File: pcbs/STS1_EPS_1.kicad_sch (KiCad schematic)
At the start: 6 parts, among them J1 Inter-EPS, U12 BD50GA5WEFJ

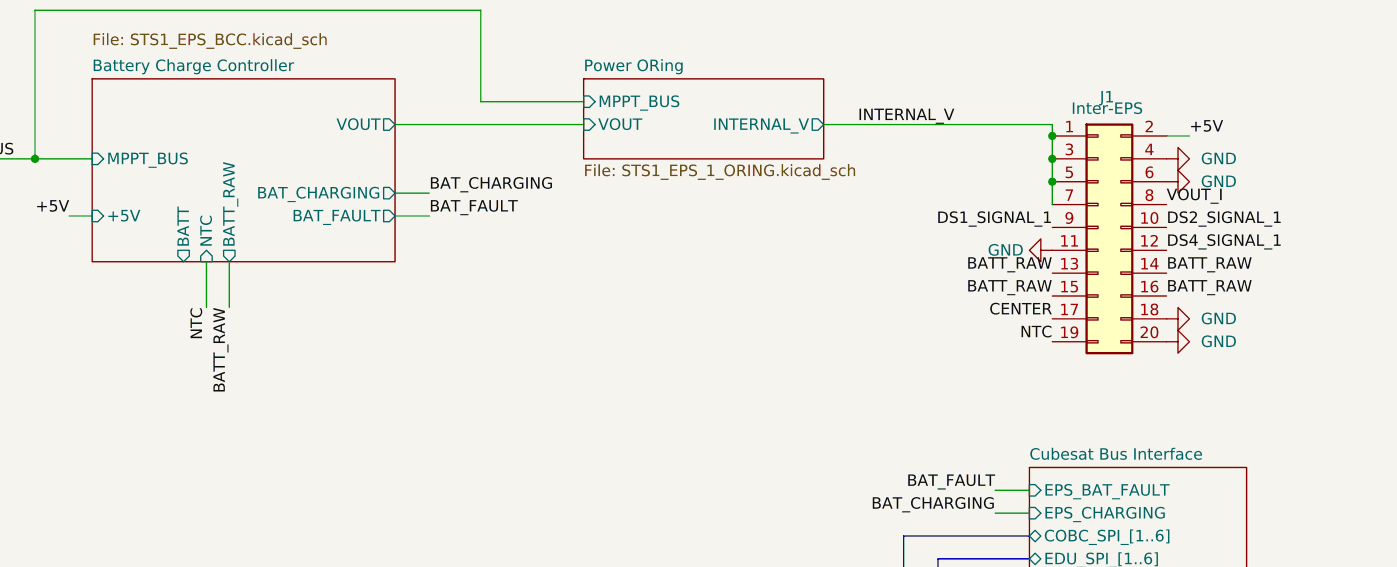
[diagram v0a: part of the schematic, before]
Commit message: Worked on STS1_EPS_1.
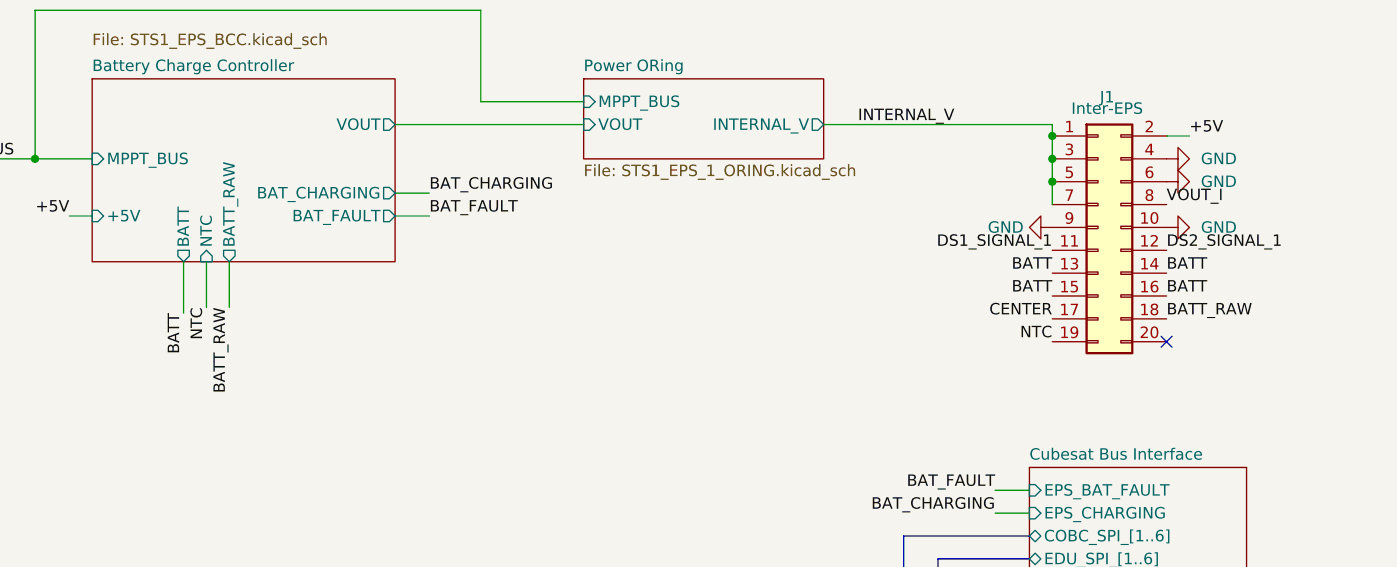
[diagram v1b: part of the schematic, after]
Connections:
- net DS4_SIGNAL_1 is gone; now on net DS2_SIGNAL_1: J1.12 (Pin_12)
- net BATT_RAW: now also J1.18 (Pin_18); no longer J1.13 (Pin_13), J1.14 (Pin_14), J1.15 (Pin_15), J1.16 (Pin_16)
- net DS1_SIGNAL_1: now also J1.11 (Pin_11); no longer J1.9 (Pin_9)
- net DS2_SIGNAL_1: no longer J1.10 (Pin_10)
- net GND: now also J1.10 (Pin_10), J1.9 (Pin_9); no longer J1.11 (Pin_11), J1.18 (Pin_18), J1.20 (Pin_20)
- new net BATT: J1.13 (Pin_13), J1.14 (Pin_14), J1.15 (Pin_15), J1.16 (Pin_16)
- no-connect marks 2 -> 3

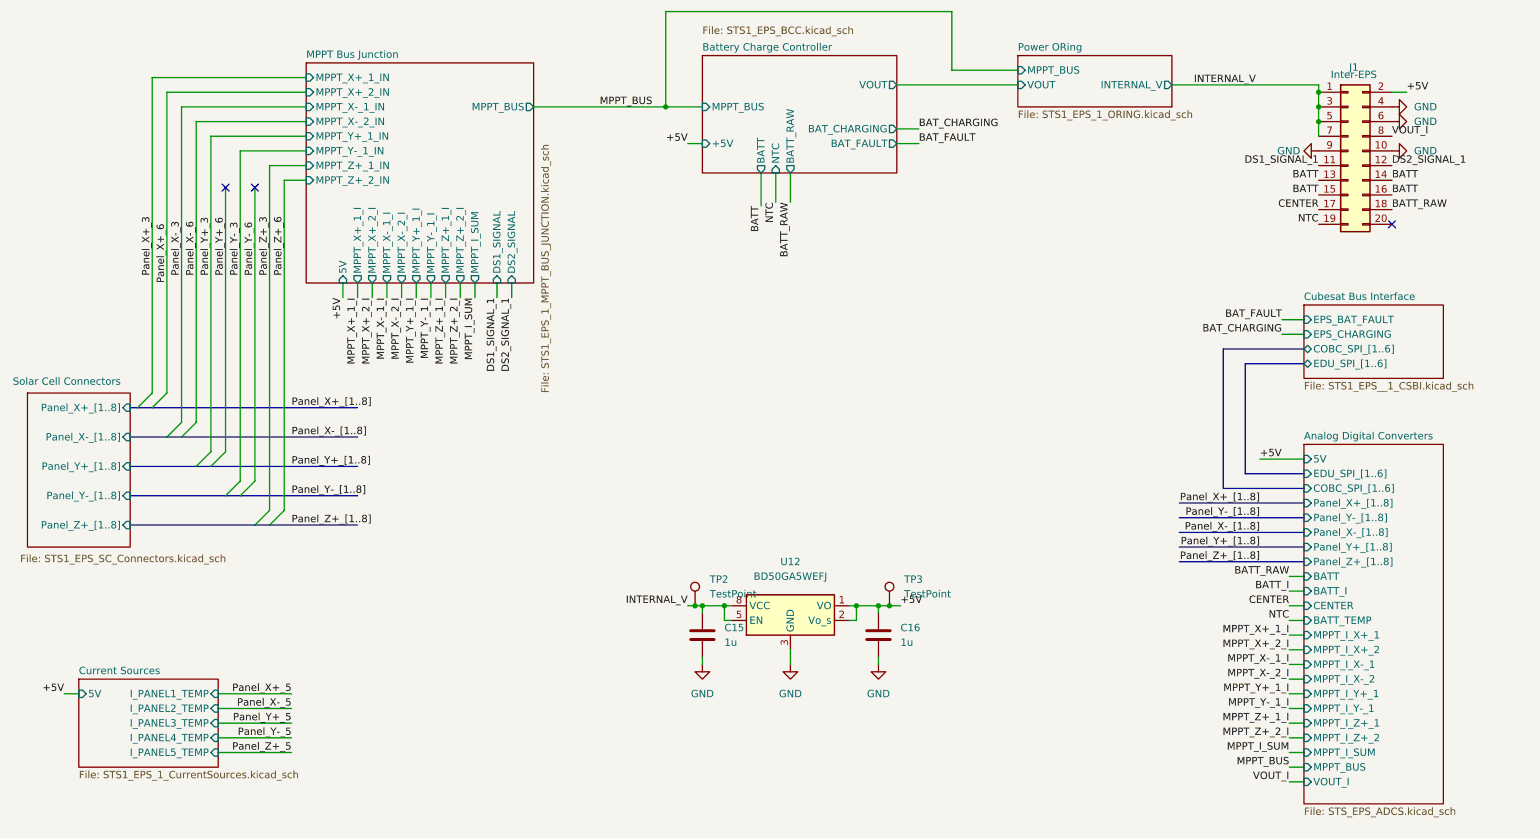
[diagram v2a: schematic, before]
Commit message: Worked on STS1_EPS_1.
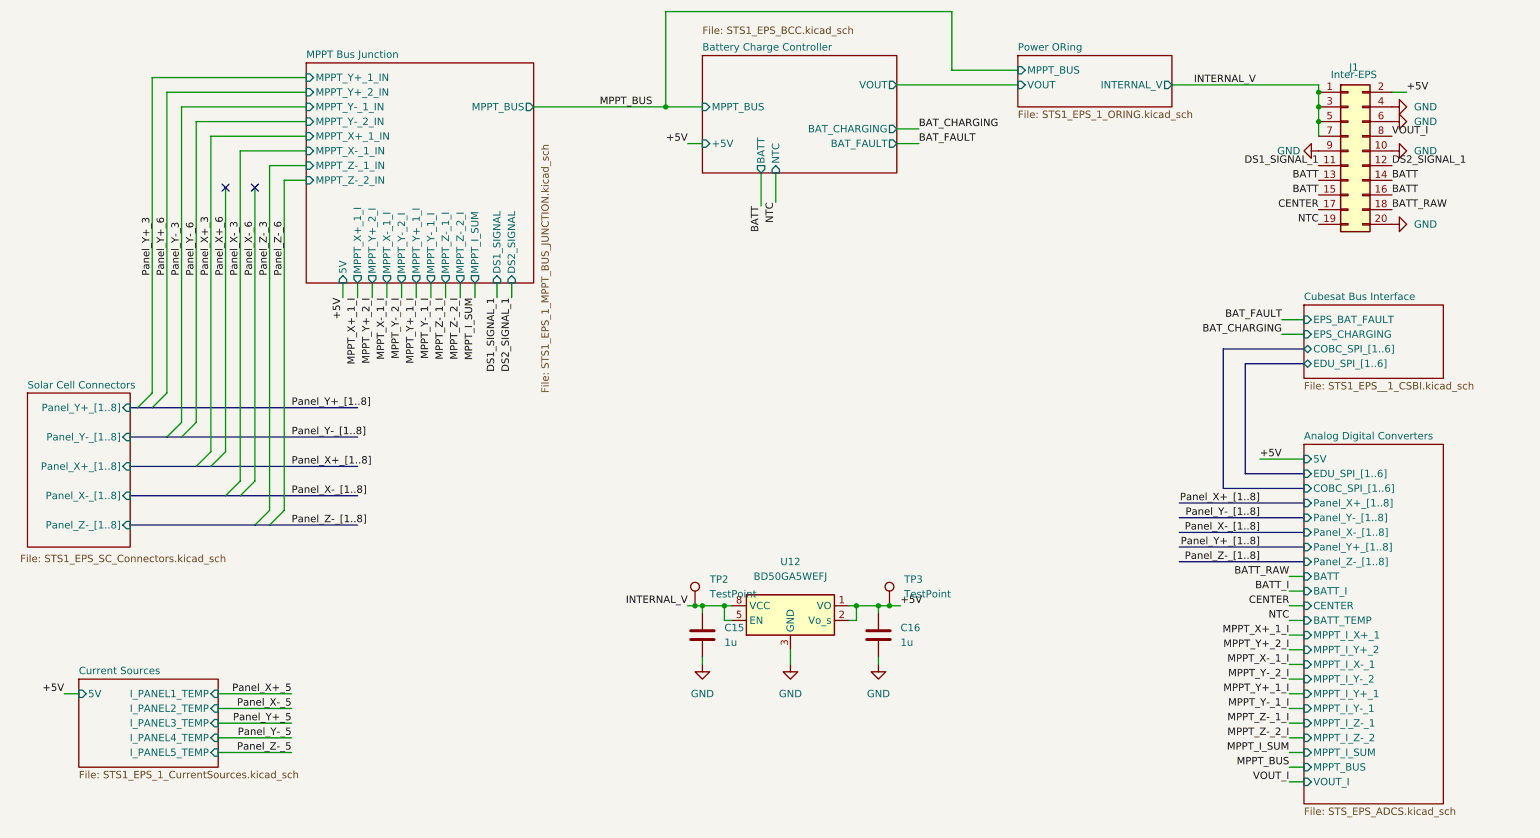
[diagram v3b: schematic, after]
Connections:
- net GND: now also J1.20 (Pin_20)
- no-connect marks 3 -> 2
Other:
- sheet Analog Digital Converters ports: added MPPT_I_Y+_2, MPPT_I_Y-_2, MPPT_I_Z-_1, MPPT_I_Z-_2, Panel_Z-_[1..8]; removed MPPT_I_X+_2, MPPT_I_X-_2, MPPT_I_Z+_1, MPPT_I_Z+_2, Panel_Z+_[1..8]
- sheet Battery Charge Controller ports: added none; removed BATT_RAW
- sheet MPPT Bus Junction ports: added MPPT_Y+_2_I, MPPT_Y+_2_IN, MPPT_Y-_2_I, MPPT_Y-_2_IN, MPPT_Z-_1_I, MPPT_Z-_1_IN, MPPT_Z-_2_I, MPPT_Z-_2_IN; removed MPPT_X+_2_I, MPPT_X+_2_IN, MPPT_X-_2_I, MPPT_X-_2_IN, MPPT_Z+_1_I, MPPT_Z+_1_IN, MPPT_Z+_2_I, MPPT_Z+_2_IN
- sheet Solar Cell Connectors ports: added Panel_Z-_[1..8]; removed Panel_Z+_[1..8]

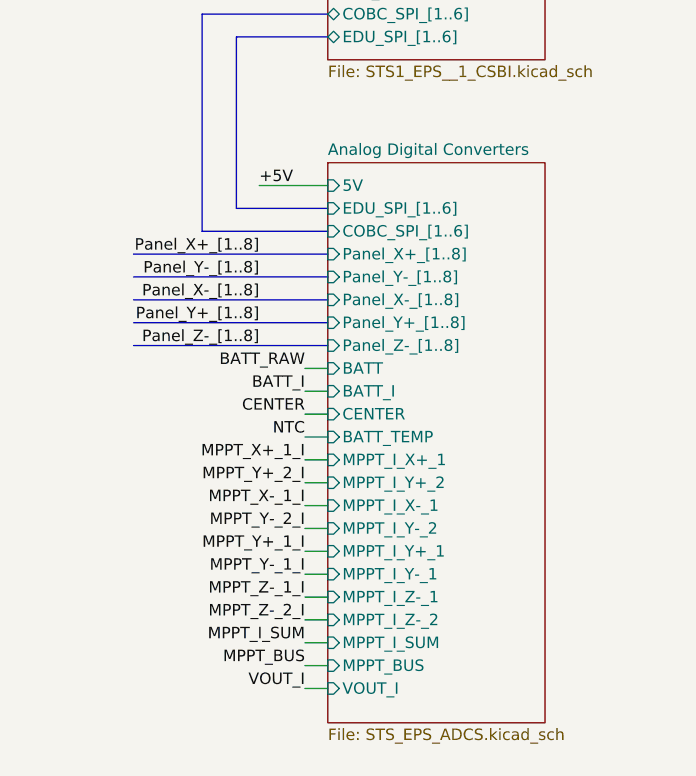
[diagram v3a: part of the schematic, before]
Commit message: Worked on STS1_EPS_1.
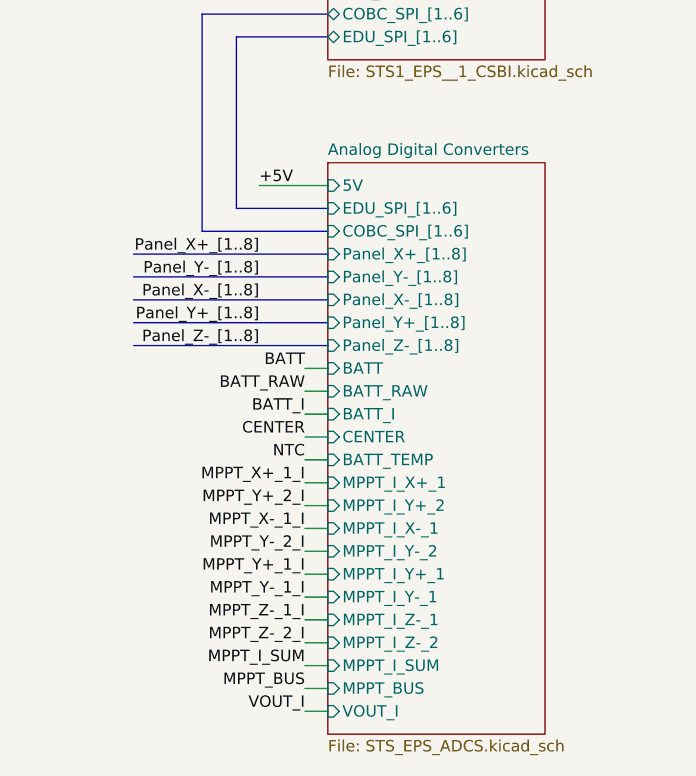
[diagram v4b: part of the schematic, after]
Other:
- sheet Analog Digital Converters ports: added BATT_RAW; removed none

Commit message: Worked on STS1_EPS_1 and STS1_EPS_2.
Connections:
- net BATT_I: now also J1.20 (Pin_20)
- net GND: no longer J1.20 (Pin_20)
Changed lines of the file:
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@@
+    (effects (font (size 1.27 1.27)) (justify left bottom))
+  )
+  (label "BATT_I" (at 250.19 54.61 0)
     (effects (font (size 1.27 1.27)) (justify left bottom))
   )
@@
     )
     (property "Datasheet" "" (id 3) (at 250.19 41.91 0)
-      (effects (font (size 1.27 1.27)) hide)
-    )
-    (pin "1")
-  )
-  (symbol (lib_id "power:GND") (at 250.19 54.61 90) (unit 1)
-    (in_bom yes) (on_board yes) (fields_autoplaced)
-    (property "Reference" "#PWR068" (id 0) (at 256.54 54.61 0)
-      (effects (font (size 1.27 1.27)) hide)
-    )
-    (property "Value" "GND" (id 1) (at 254 54.6099 90)
-      (effects (font (size 1.27 1.27)) (justify right))
-    )
-    (property "Footprint" "" (id 2) (at 250.19 54.61 0)
-      (effects (font (size 1.27 1.27)) hide)
-    )
-    (property "Datasheet" "" (id 3) (at 250.19 54.61 0)
       (effects (font (size 1.27 1.27)) hide)
     )
@@
       (reference "#PWR067") (unit 1) (value "GND") (footprint "")
     )
-    (path "/5715810c-7aee-4fb7-8ca7-e5bcf3201e81"
-      (reference "#PWR068") (unit 1) (value "GND") (footprint "")
-    )
     (path "/1fa7f756-57e9-4cd3-900e-1a1c84a07cba/6a3f3e97-3980-4780-a8e9-1ce1471695d7"

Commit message: Added a logic voltage, so that the deployment circuit breaker FETs also work, when battery is fails.
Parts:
- J1: footprint Connector_PinHeader_2.00mm:PinHeader_2x10_P2.00mm_Vertical -> Connector_PinHeader_2.00mm:PinHeader_2x11_P2.00mm_Vertical; symbol Connector_Generic:Conn_02x10_Odd_Even -> Connector_Generic:Conn_02x11_Odd_Even
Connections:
- new net MPPT_SUM: J1.22 (Pin_22)
- new net V_LOGIC: J1.21 (Pin_21)
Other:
- sheet MPPT Bus Junction ports: added MPPT_SUM; removed none
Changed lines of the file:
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@@
+    (stroke (width 0) (type default) (color 0 0 0 0))
+  )
+  (wire (pts (xy 101.6 36.83) (xy 103.505 36.83))
     (stroke (width 0) (type default) (color 0 0 0 0))
   )
@@
     (effects (font (size 1.27 1.27)) (justify right bottom))
   )
+  (label "MPPT_SUM" (at 250.19 57.15 0)
+    (effects (font (size 1.27 1.27)) (justify left bottom))
+  )
   (label "MPPT_X-_1_I" (at 76.2 67.31 270)
     (effects (font (size 1.27 1.27)) (justify right bottom))
@@
     (effects (font (size 1.27 1.27)) (justify left bottom))
   )
+  (label "MPPT_SUM" (at 103.505 36.83 0)
+    (effects (font (size 1.27 1.27)) (justify left bottom))
+  )
   (label "BATT_RAW" (at 232.41 118.11 180)
     (effects (font (size 1.27 1.27)) (justify right bottom))
@@
   (label "DS2_SIGNAL_1" (at 250.19 44.45 0)
     (effects (font (size 1.27 1.27)) (justify left bottom))
+  )
+  (label "V_LOGIC" (at 237.49 57.15 180)
+    (effects (font (size 1.27 1.27)) (justify right bottom))
   )
   (label "Panel_Y-_5" (at 59.69 143.51 180)
@@
     (pin "1")
   )
-  (symbol (lib_id "Connector_Generic:Conn_02x10_Odd_Even") (at 242.57 41.91 0) (unit 1)
+  (symbol (lib_id "Connector_Generic:Conn_02x11_Odd_Even") (at 242.57 44.45 0) (unit 1)
     (in_bom yes) (on_board yes)
-    (property "Reference" "J1" (id 0) (at 243.586 27.432 0))
-    (property "Value" "Inter-EPS" (id 1) (at 243.586 28.702 0))
-    (property "Footprint" "Connector_PinHeader_2.00mm:PinHeader_2x10_P2.00mm_Vertical" (id 2) (at 242.57 41.91 0)
-      (effects (font (size 1.27 1.27)) hide)
-    )
-    (property "Datasheet" "~" (id 3) (at 242.57 41.91 0)
-      (effects (font (size 1.27 1.27)) hide)
-    )
-    (property "Part#" "ESQT-107-02-F-D-800" (id 4) (at 242.57 41.91 0)
+    (property "Reference" "J1" (id 0) (at 243.84 27.305 0))
+    (property "Value" "Inter-EPS" (id 1) (at 243.84 29.21 0))
+    (property "Footprint" "Connector_PinHeader_2.00mm:PinHeader_2x11_P2.00mm_Vertical" (id 2) (at 242.57 44.45 0)
+      (effects (font (size 1.27 1.27)) hide)
+    )
+    (property "Datasheet" "~" (id 3) (at 242.57 44.45 0)
+      (effects (font (size 1.27 1.27)) hide)
+    )
+    (property "Part#" "ESQT-107-02-F-D-800" (id 4) (at 242.57 44.45 0)
       (effects (font (size 1.27 1.27)) hide)
     )
@@
     (pin "2")
     (pin "20")
+    (pin "21")
+    (pin "22")
     (pin "3")
     (pin "4")
@@
       (effects (font (size 1.27 1.27)) (justify left bottom))
     )
-    (property "Sheet file" "STS1_EPS_1_MPPT_BUS_JUNCTION.kicad_sch" (id 1) (at 102.87 83.82 90)
+    (property "Sheet file" "STS1_EPS_1_MPPT_BUS_JUNCTION.kicad_sch" (id 1) (at 102.235 92.075 90)
       (effects (font (size 1.27 1.27)) (justify left top))
     )
@@
     (pin "DS2_SIGNAL" input (at 97.79 64.77 270)
       (effects (font (size 1.27 1.27)) (justify left))
+    )
+    (pin "MPPT_SUM" output (at 101.6 36.83 0)
+      (effects (font (size 1.27 1.27)) (justify right))
     )
   )
@@
     )
     (path "/ded3cad6-377c-4d68-8742-ee2e9e416717"
-      (reference "J1") (unit 1) (value "Inter-EPS") (footprint "Connector_PinHeader_2.00mm:PinHeader_2x10_P2.00mm_Vertical")
+      (reference "J1") (unit 1) (value "Inter-EPS") (footprint "Connector_PinHeader_2.00mm:PinHeader_2x11_P2.00mm_Vertical")
     )
     (path "/0b54958e-6712-400f-aa61-9f5fa371c31d/acef06f6-89af-43de-b708-bb39af44e566"

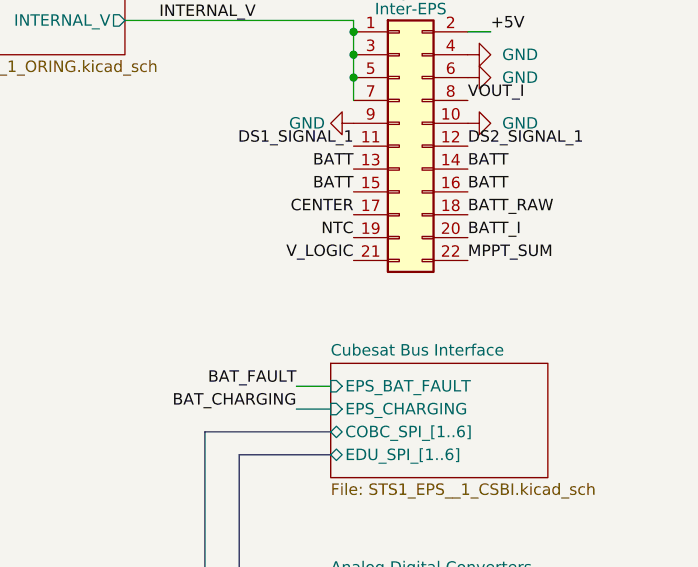
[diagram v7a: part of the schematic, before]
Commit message: Added part numbers to CSBI and inter EPS connectors. Also added some missing 3d files.
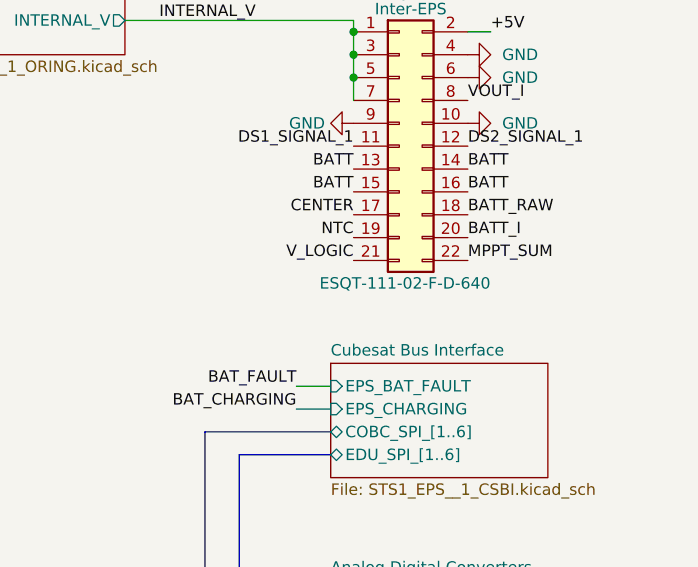
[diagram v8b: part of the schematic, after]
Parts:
- J1: Part# ESQT-107-02-F-D-800 -> ESQT-111-02-F-D-640
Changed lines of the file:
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@@
       (effects (font (size 1.27 1.27)) hide)
     )
-    (property "Part#" "ESQT-107-02-F-D-800" (id 4) (at 242.57 44.45 0)
-      (effects (font (size 1.27 1.27)) hide)
-    )
+    (property "Part#" "ESQT-111-02-F-D-640" (id 4) (at 243.205 59.69 0))
     (pin "1")
     (pin "10")
@@
     )
     (path "/1f2aab95-1ce2-4d7d-8e47-47ae14e38d9e/00000000-0000-0000-0000-00006179b797"
-      (reference "CSBI_1") (unit 1) (value "ESQT-125-02-F-D-800") (footprint "Connector_PinHeader_2.00mm:PinHeader_2x25_P2.00mm_Vertical")
+      (reference "CSBI_1") (unit 1) (value "ESQT-125-02-F-D-640") (footprint "Connector_PinHeader_2.00mm:PinHeader_2x25_P2.00mm_Vertical")
     )
     (path "/1f2aab95-1ce2-4d7d-8e47-47ae14e38d9e/00000000-0000-0000-0000-0000617ab6cd"
-      (reference "CSBI_2") (unit 1) (value "ESQT-125-02-F-D-800") (footprint "Connector_PinHeader_2.00mm:PinHeader_2x25_P2.00mm_Vertical")
+      (reference "CSBI_2") (unit 1) (value "ESQT-125-02-F-D-640") (footprint "Connector_PinHeader_2.00mm:PinHeader_2x25_P2.00mm_Vertical")
     )
     (path "/3f2412fd-ceb3-4d5f-b693-7628adb9c64f/94825378-4abf-4605-a44d-ce5a98bab42f"
@@
     )
     (path "/3f2412fd-ceb3-4d5f-b693-7628adb9c64f/3b8240d2-4008-4a93-b05d-8d239444b308"
-      (reference "R7") (unit 1) (value "500k") (footprint "Resistor_SMD:R_0805_2012Metric")
+      (reference "R7") (unit 1) (value "499k") (footprint "Resistor_SMD:R_0805_2012Metric")
     )
     (path "/3f2412fd-ceb3-4d5f-b693-7628adb9c64f/f458de1e-ae9b-4650-9d23-8e3e2b2b59c3"
@@
     )
     (path "/3f2412fd-ceb3-4d5f-b693-7628adb9c64f/4121c95f-530f-4852-92e0-9f75d7af4926"
-      (reference "R9") (unit 1) (value "166k") (footprint "Resistor_SMD:R_0805_2012Metric")
+      (reference "R9") (unit 1) (value "169k") (footprint "Resistor_SMD:R_0805_2012Metric")
     )
     (path "/3f2412fd-ceb3-4d5f-b693-7628adb9c64f/2b84e897-05d2-47fa-b5db-a7f9425518f6"
@@
     )
     (path "/1fa7f756-57e9-4cd3-900e-1a1c84a07cba/4f4fa1eb-492d-404d-b7dd-002a78e82a53"
-      (reference "R24") (unit 1) (value "87k5") (footprint "Resistor_SMD:R_0805_2012Metric")
+      (reference "R24") (unit 1) (value "86k6") (footprint "Resistor_SMD:R_0805_2012Metric")
     )
     (path "/1fa7f756-57e9-4cd3-900e-1a1c84a07cba/b0917f33-35b4-44e8-983e-3d1f6ba9470a"
@@
     )
     (path "/1fa7f756-57e9-4cd3-900e-1a1c84a07cba/e38bd244-a496-4946-b121-0ffdb72633a8"
-      (reference "R52") (unit 1) (value "87k5") (footprint "Resistor_SMD:R_0805_2012Metric")
+      (reference "R52") (unit 1) (value "86k6") (footprint "Resistor_SMD:R_0805_2012Metric")
     )
     (path "/1fa7f756-57e9-4cd3-900e-1a1c84a07cba/65588c33-cbaf-48da-984b-d8c1b3dc2ee0"
